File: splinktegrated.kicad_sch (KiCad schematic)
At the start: 55 parts, among them J1 USB_C_Receptacle_USB2.0, J10 NA_Ribbon, J11 NA_Serial, J12 NA_Conn_01x04_Female, J14 Cirque, J2 NA_Conn_01x04_Female, J3 NA_Conn_01x04_Female, J4 NA_Conn_01x04_Female, J5 Conn_01x02, J6 Cirque, J7 NA_trackball, J8 NA_Ribbon, J9 NA_RGB, SW1 NA_SW_SPST, SW2 NA_SW_SPST, U1 RP2040, U2 USBLC6-2P6, U3 XC6210B332MR-G, U4 USBLC6-2P6, U5 W25Q128JVS, Y1 Crystal_GND24

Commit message: add second jumper for full duplex
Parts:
- added NA_JP3, NA_JP4: NA_Jumper_2_Open, local-libraries:SolderJumper-2_P1.3mm_Open_RoundedPad1.0x1.5mm, symbol Jumper:Jumper_2_Open
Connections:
- net D12: now reaches U1.15 (GPIO12)
- net D12: now also NA_JP3.2 (B), NA_JP4.2 (B)
- net at NA_J6.T, NA_JP1.1 (A): now also J11.S, NA_JP4.1 (A)
- net at J11.T, NA_JP2.1 (A): now also NA_J6.S, NA_JP3.1 (A)
- no-connect marks 23 -> 20
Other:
- moved on the sheet: NA_JP1

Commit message: start implementing vik
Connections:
- net +3V3: no longer J6.1 (Pin_1)
- net GND: now also J6.11 (Pin_11); no longer J6.6 (Pin_6), J6.7 (Pin_7)
- net miso_l: now also J6.2 (Pin_2); no longer J6.5 (Pin_5), J6.8 (Pin_8)
- net mosi_l: now also J6.5 (Pin_5); no longer J6.10 (Pin_10), J6.3 (Pin_3)
- net rgb_r: now also J6.8 (Pin_8)
- net sc_l: now also J6.1 (Pin_1); no longer J6.4 (Pin_4), J6.9 (Pin_9)
- net ss_l: no longer J6.11 (Pin_11), J6.2 (Pin_2)
- net SDA: now reaches U1.4 (GPIO2)
- net SDA: now also J6.9 (Pin_9)
- net SCL: now reaches U1.5 (GPIO3)
- net SCL: now also J6.10 (Pin_10)
- no-connect marks 20 -> 19
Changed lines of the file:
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@@
 	)
 	(no_connect
-		(at 182.88 63.5)
-	)
-	(no_connect
-		(at 182.88 66.04)
-	)
-	(no_connect
 		(at 431.8 64.77)
 	)
@@
 		(at 391.16 67.31)
 	)
+	(no_connect
+		(at 431.8 46.99)
+	)
 	(polyline
 		(pts
@@
 	(global_label "ss_l"
 		(shape input)
-		(at 431.8 59.69 180)
+		(at 469.9 59.69 180)
 		(effects
 			(font
@@
 		)
 		(property "Intersheetrefs" "${INTERSHEET_REFS}"
-			(at 427.3307 59.6106 0)
+			(at 465.4307 59.6106 0)
 			(effects
 				(font
@@
 	(global_label "miso_l"
 		(shape input)
-		(at 431.8 44.45 180)
+		(at 431.8 59.69 180)
 		(effects
 			(font
@@
 		)
 		(property "Intersheetrefs" "${INTERSHEET_REFS}"
-			(at 424.9117 44.3706 0)
+			(at 424.9117 59.6106 0)
 			(effects
 				(font
@@
 	(global_label "mosi_l"
 		(shape input)
-		(at 431.8 57.15 180)
+		(at 469.9 57.15 180)
 		(effects
 			(font
@@
 		)
 		(property "Intersheetrefs" "${INTERSHEET_REFS}"
-			(at 424.9117 57.0706 0)
+			(at 463.0117 57.0706 0)
 			(effects
 				(font
@@
 		)
 	)
+	(global_label "SDA"
+		(shape input)
+		(at 182.88 63.5 0)
+		(effects
+			(font
+				(size 1.27 1.27)
+			)
+			(justify left)
+		)
+		(property "Intersheetrefs" "${INTERSHEET_REFS}"
+			(at 212.09 118.11 0)
+			(effects
+				(font
+					(size 1.27 1.27)
+				)
+				(hide yes)
+			)
+		)
+	)
 	(global_label "col3_l"
 		(shape input)
@@
 		)
 	)
+	(global_label "rgb_r"
+		(shape input)
+		(at 431.8 44.45 180)
+		(effects
+			(font
+				(size 1.27 1.27)
+			)
+			(justify right)
+		)
+		(property "Intersheetrefs" "${INTERSHEET_REFS}"
+			(at 344.17 -22.86 0)
+			(effects
+				(font
+					(size 1.27 1.27)
+				)
+				(hide yes)
+			)
+		)
+	)
 	(global_label "ss_l"
 		(shape input)
@@
 	(global_label "sc_l"
 		(shape input)
-		(at 431.8 41.91 180)
+		(at 431.8 62.23 180)
 		(effects
 			(font
@@
 		)
 		(property "Intersheetrefs" "${INTERSHEET_REFS}"
-			(at 427.2702 41.8306 0)
+			(at 427.2702 62.1506 0)
 			(effects
 				(font
@@
 		)
 	)
+	(global_label "SDA"
+		(shape input)
+		(at 431.8 41.91 180)
+		(effects
+			(font
+				(size 1.27 1.27)
+			)
+			(justify right)
+		)
+		(property "Intersheetrefs" "${INTERSHEET_REFS}"
+			(at 402.59 -12.7 0)
+			(effects
+				(font
+					(size 1.27 1.27)
+				)
+				(hide yes)
+			)
+		)
+	)
 	(global_label "sc_l"
 		(shape input)
-		(at 431.8 54.61 180)
+		(at 469.9 54.61 180)
 		(effects
 			(font
@@
 		)
 		(property "Intersheetrefs" "${INTERSHEET_REFS}"
-			(at 427.2702 54.5306 0)
+			(at 465.3702 54.5306 0)
 			(effects
 				(font
@@
 		)
 	)
+	(global_label "SCL"
+		(shape input)
+		(at 182.88 66.04 0)
+		(effects
+			(font
+				(size 1.27 1.27)
+			)
+			(justify left)
+		)
+		(property "Intersheetrefs" "${INTERSHEET_REFS}"
+			(at 212.09 120.65 0)
+			(effects
+				(font
+					(size 1.27 1.27)
+				)
+				(hide yes)
+			)
+		)
+	)
 	(global_label "mosi_l"
 		(shape input)
-		(at 431.8 39.37 180)
+		(at 431.8 52.07 180)
 		(effects
 			(font
@@
 		)
 		(property "Intersheetrefs" "${INTERSHEET_REFS}"
-			(at 424.9117 39.2906 0)
+			(at 424.9117 51.9906 0)
 			(effects
 				(font
@@
 	(global_label "miso_l"
 		(shape input)
-		(at 431.8 52.07 180)
+		(at 469.9 52.07 180)
 		(effects
 			(font
@@
 		)
 		(property "Intersheetrefs" "${INTERSHEET_REFS}"
-			(at 424.9117 51.9906 0)
+			(at 463.0117 51.9906 0)
 			(effects
 				(font
@@
 		)
 	)
+	(global_label "SCL"
+		(shape input)
+		(at 431.8 39.37 180)
+		(effects
+			(font
+				(size 1.27 1.27)
+			)
+			(justify right)
+		)
+		(property "Intersheetrefs" "${INTERSHEET_REFS}"
+			(at 402.59 -15.24 0)
+			(effects
+				(font
+					(size 1.27 1.27)
+				)
+				(hide yes)
+			)
+		)
+	)
 	(global_label "row3_l"
 		(shape input)
@@
 	(global_label "ss_l"
 		(shape input)
-		(at 431.8 36.83 180)
+		(at 469.9 36.83 180)
 		(effects
 			(font
@@
 		)
 		(property "Intersheetrefs" "${INTERSHEET_REFS}"
-			(at 427.3307 36.7506 0)
+			(at 465.4307 36.7506 0)
 			(effects
 				(font
@@
 	(symbol
 		(lib_id "power:GND")
-		(at 431.8 49.53 270)
+		(at 469.9 49.53 270)
 		(unit 1)
 		(exclude_from_sim no)
@@
 		(dnp no)
 		(property "Reference" "#PWR039"
-			(at 425.45 49.53 0)
+			(at 463.55 49.53 0)
 			(effects
 				(font
@@
 		)
 		(property "Value" "GND"
-			(at 425.45 49.53 90)
+			(at 463.55 49.53 90)
 			(effects
 				(font
@@
 		)
 		(property "Footprint" ""
-			(at 431.8 49.53 0)
+			(at 469.9 49.53 0)
 			(effects
 				(font
@@
 		)
 		(property "Datasheet" ""
-			(at 431.8 49.53 0)
+			(at 469.9 49.53 0)
 			(effects
 				(font
@@
 		)
 		(property "Description" ""
-			(at 431.8 49.53 0)
+			(at 469.9 49.53 0)
 			(effects
 				(font
@@
 	(symbol
 		(lib_id "power:GND")
-		(at 431.8 46.99 270)
+		(at 431.8 36.83 270)
 		(unit 1)
 		(exclude_from_sim no)
@@
 		(dnp no)
 		(property "Reference" "#PWR037"
-			(at 425.45 46.99 0)
+			(at 425.45 36.83 0)
 			(effects
 				(font
@@
 		)
 		(property "Value" "GND"
-			(at 425.45 46.99 90)
+			(at 425.45 36.83 90)
 			(effects
 				(font
@@
 		)
 		(property "Footprint" ""
-			(at 431.8 46.99 0)
+			(at 431.8 36.83 0)
 			(effects
 				(font
@@
 		)
 		(property "Datasheet" ""
-			(at 431.8 46.99 0)
+			(at 431.8 36.83 0)
 			(effects
 				(font
@@
 		)
 		(property "Description" ""
-			(at 431.8 46.99 0)
+			(at 431.8 36.83 0)
 			(effects
 				(font
@@
 	(symbol
 		(lib_id "power:+3.3V")
-		(at 431.8 62.23 90)
+		(at 458.47 69.85 90)
 		(unit 1)
 		(exclude_from_sim no)
@@
 		(dnp no)
 		(property "Reference" "#PWR040"
-			(at 435.61 62.23 0)
+			(at 462.28 69.85 0)
 			(effects
 				(font
@@
 		)
 		(property "Value" "+3V3"
-			(at 427.99 62.23 0)
+			(at 461.01 69.85 0)
 			(effects
 				(font
@@
 		)
 		(property "Footprint" ""
-			(at 431.8 62.23 0)
+			(at 458.47 69.85 0)
 			(effects
 				(font
@@
 		)
 		(property "Datasheet" ""
-			(at 431.8 62.23 0)
+			(at 458.47 69.85 0)
 			(effects
 				(font
@@
 		)
 		(property "Description" ""
-			(at 431.8 62.23 0)
+			(at 458.47 69.85 0)
 			(effects
 				(font

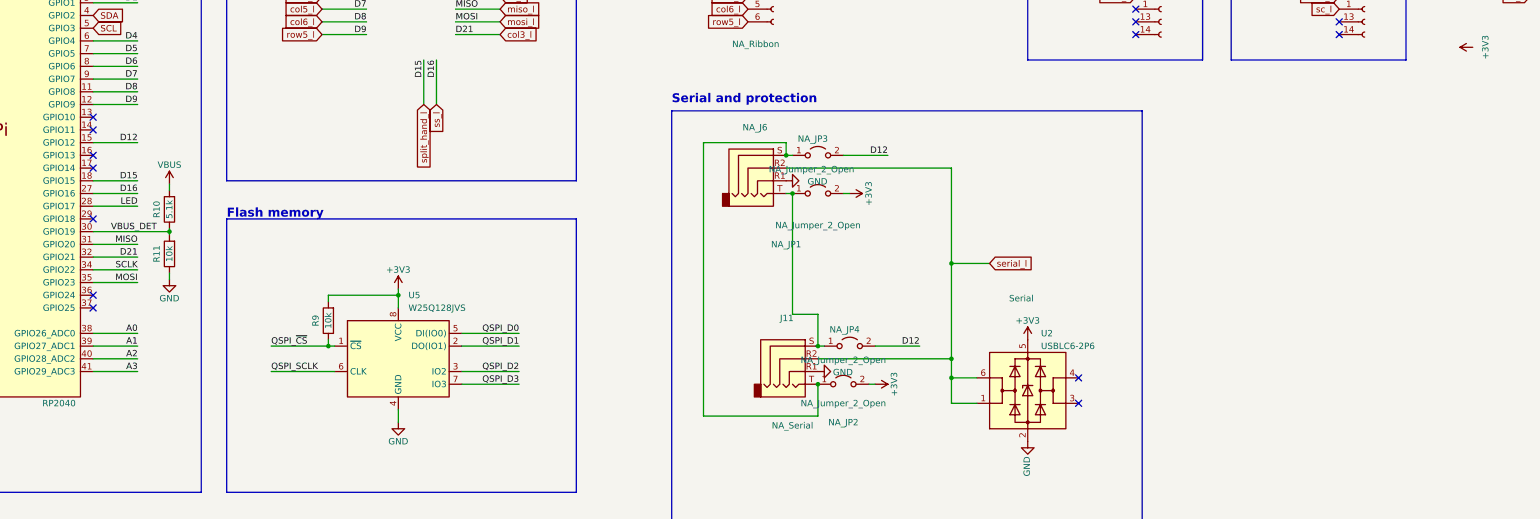
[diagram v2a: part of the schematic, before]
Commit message: add criss crossed jumpers for full duplex
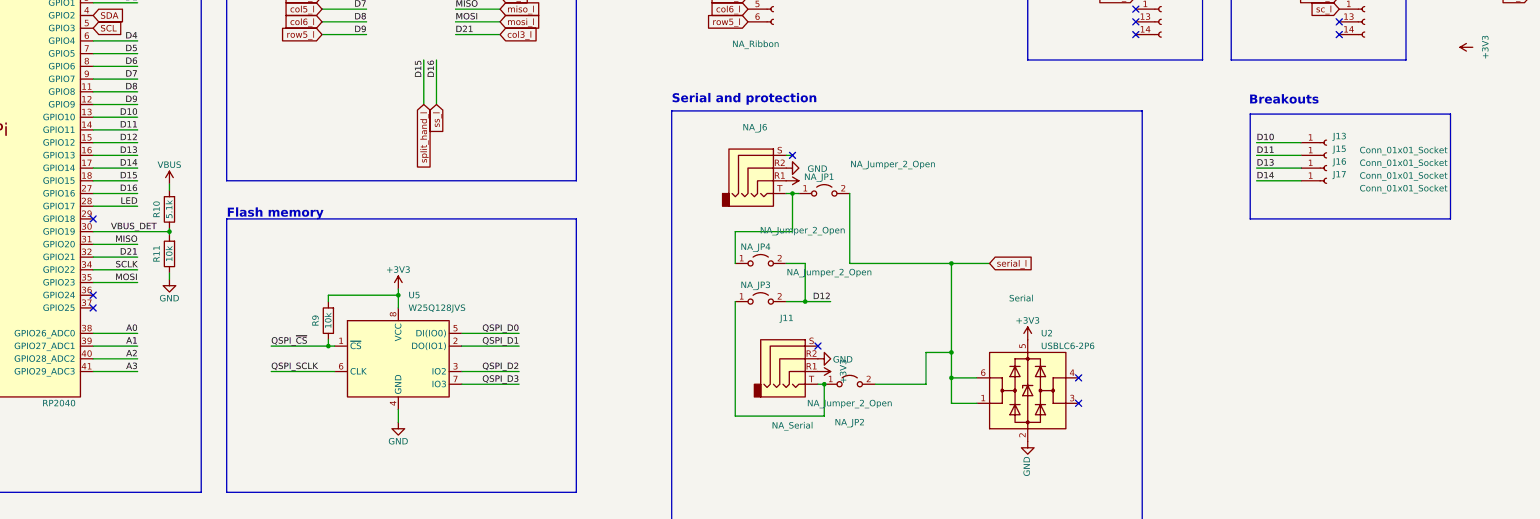
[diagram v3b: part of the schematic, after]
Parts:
- added J13, J15, J16, J17: Conn_01x01_Socket, local-libraries:PinHeader_1x01_P1.27mm_Vertical, symbol Connector:Conn_01x01_Socket
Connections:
- net +3V3: now also J11.R1, NA_J6.R1; no longer NA_JP1.2 (B), NA_JP2.2 (B)
- net GND: now also J11.R2, NA_J6.R2; no longer J11.R1, NA_J6.R1
- net serial_l: now also NA_JP1.2 (B), NA_JP2.2 (B); no longer J11.R2, NA_J6.R2
- net D10: now reaches U1.13 (GPIO10)
- net D10: now also J13.1 (Pin_1)
- net D11: now reaches U1.14 (GPIO11)
- net D11: now also J15.1 (Pin_1)
- net D13: now reaches U1.16 (GPIO13)
- net D13: now also J16.1 (Pin_1)
- net D14: now reaches U1.17 (GPIO14)
- net D14: now also J17.1 (Pin_1)
- net at NA_J6.T, NA_JP1.1 (A), NA_JP4.1 (A): no longer J11.S
- net at J11.T, NA_JP2.1 (A), NA_JP3.1 (A): no longer NA_J6.S
- no-connect marks 19 -> 17
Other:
- note added: "Breakouts"
- moved on the sheet: NA_JP2, NA_JP3, NA_JP4

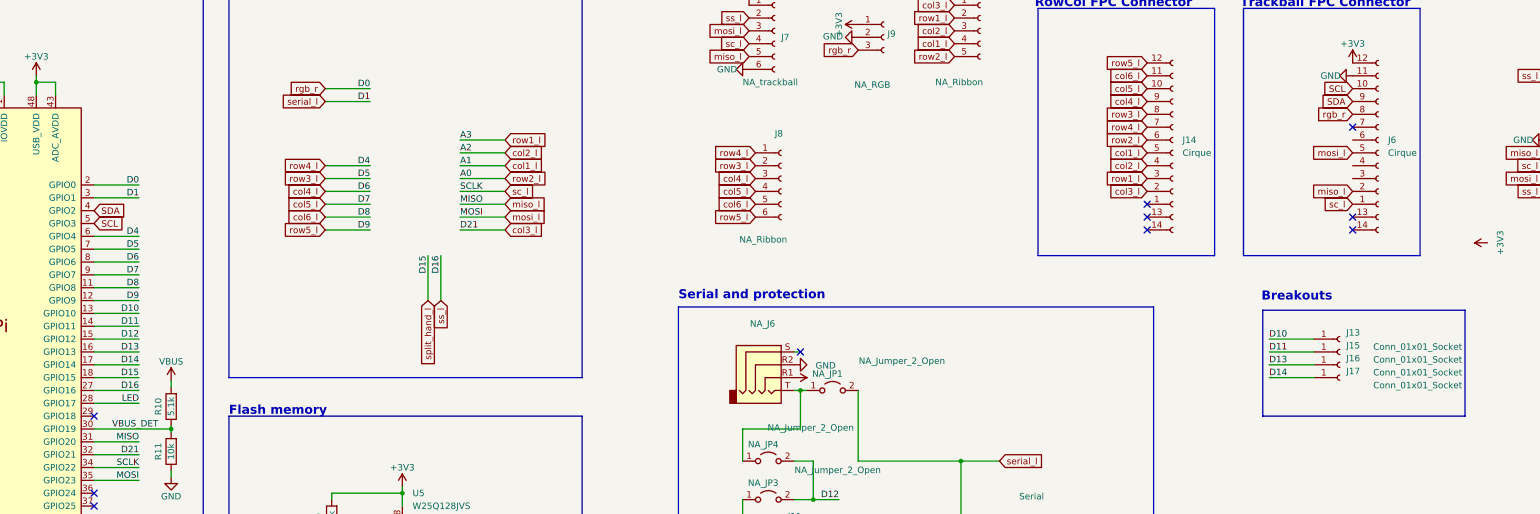
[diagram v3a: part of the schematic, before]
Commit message: add 5v jumper
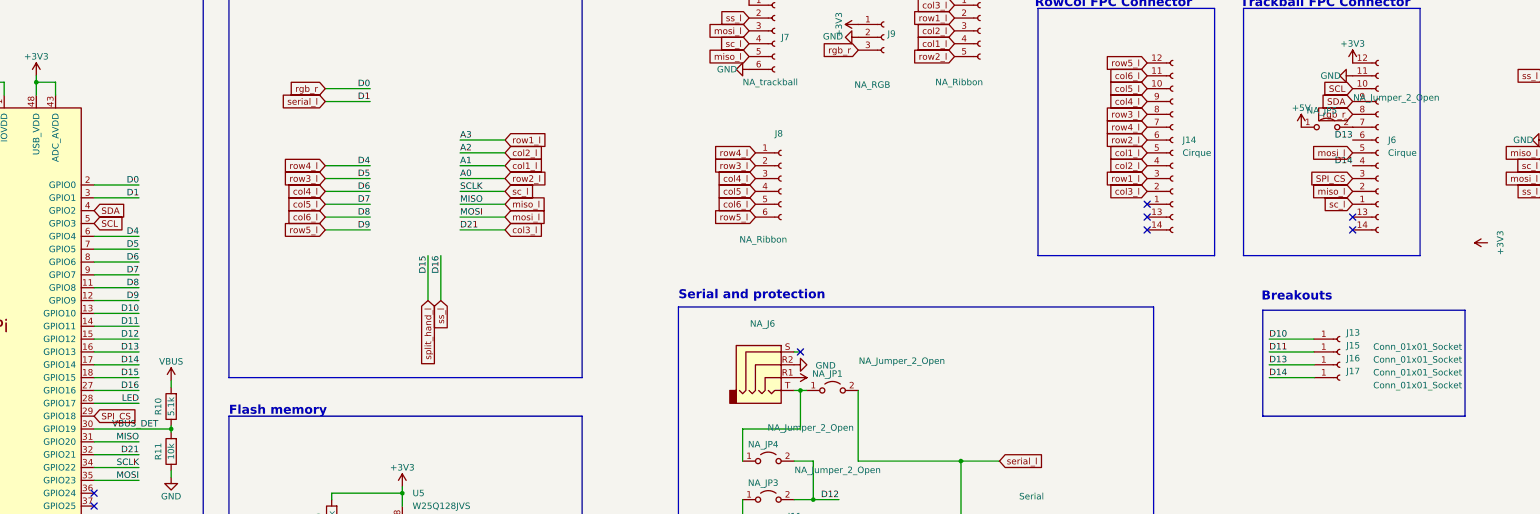
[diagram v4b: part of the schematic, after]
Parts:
- added NA_JP5: NA_Jumper_2_Open, local-libraries:SolderJumper-2_P1.3mm_Open_RoundedPad1.0x1.5mm, symbol Jumper:Jumper_2_Open
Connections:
- net +5V: now also NA_JP5.1 (A)
- net D13: now also J6.6 (Pin_6)
- net D14: now also J6.4 (Pin_4)
- net SPI_CS: now reaches U1.29 (GPIO18)
- net SPI_CS: now also J6.3 (Pin_3)
- net at J6.7 (Pin_7): now also NA_JP5.2 (B)
- no-connect marks 17 -> 15
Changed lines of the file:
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@@
 	)
 	(no_connect
-		(at 182.88 104.14)
-	)
-	(no_connect
 		(at 391.16 62.23)
 	)
@@
 		(at 391.16 67.31)
 	)
-	(no_connect
-		(at 431.8 46.99)
-	)
 	(polyline
 		(pts
@@
 		)
 	)
+	(label "D13"
+		(at 431.8 49.53 180)
+		(fields_autoplaced yes)
+		(effects
+			(font
+				(size 1.27 1.27)
+			)
+			(justify right bottom)
+		)
+	)
 	(label "QSPI_D2"
 		(at 111.76 68.58 0)
@@
 		)
 	)
+	(label "D14"
+		(at 431.8 54.61 180)
+		(fields_autoplaced yes)
+		(effects
+			(font
+				(size 1.27 1.27)
+			)
+			(justify right bottom)
+		)
+	)
 	(label "D+_daughter"
 		(at -66.675 87.63 180)
@@
 		)
 	)
+	(global_label "SPI_CS"
+		(shape input)
+		(at 431.8 57.15 180)
+		(effects
+			(font
+				(size 1.27 1.27)
+			)
+			(justify right)
+		)
+		(property "Intersheetrefs" "${INTERSHEET_REFS}"
+			(at 402.59 17.78 0)
+			(effects
+				(font
+					(size 1.27 1.27)
+				)
+				(hide yes)
+			)
+		)
+	)
 	(global_label "col4_l"
 		(shape input)
@@
 		)
 	)
+	(global_label "SPI_CS"
+		(shape input)
+		(at 182.88 104.14 0)
+		(effects
+			(font
+				(size 1.27 1.27)
+			)
+			(justify left)
+		)
+		(property "Intersheetrefs" "${INTERSHEET_REFS}"
+			(at 212.09 143.51 0)
+			(effects
+				(font
+					(size 1.27 1.27)
+				)
+				(hide yes)
+			)
+		)
+	)
 	(global_label "row2_l"
 		(shape input)
@@
 	)
 	(symbol
+		(lib_id "power:+5V")
+		(at 421.64 46.99 0)
+		(unit 1)
+		(exclude_from_sim no)
+		(in_bom yes)
+		(on_board yes)
+		(dnp no)
+		(property "Reference" "#PWR041"
+			(at 421.64 50.8 0)
+			(effects
+				(font
+					(size 1.27 1.27)
+				)
+				(hide yes)
+			)
+		)
+		(property "Value" "+5V"
+			(at 421.64 43.18 0)
+			(effects
+				(font
+					(size 1.27 1.27)
+				)
+			)
+		)
+		(property "Footprint" ""
+			(at 421.64 46.99 0)
+			(effects
+				(font
+					(size 1.27 1.27)
+				)
+				(hide yes)
+			)
+		)
+		(property "Datasheet" ""
+			(at 421.64 46.99 0)
+			(effects
+				(font
+					(size 1.27 1.27)
+				)
+				(hide yes)
+			)
+		)
+		(property "Description" ""
+			(at 421.64 46.99 0)
+			(effects
+				(font
+					(size 1.27 1.27)
+				)
+				(hide yes)
+			)
+		)
+		(pin "1"
+		)
+		(instances
+			(project "splinktegrated"
+				(path "/7353e96a-343a-4876-b497-b1d205a14d97"
+					(reference "#PWR041")
+					(unit 1)
+				)
+			)
+		)
+	)
+	(symbol
 		(lib_id "Connector:Conn_01x04_Female")
 		(at 41.91 40.005 0)
@@
 					(unit 1)
 				)
+			)
+		)
+	)
+	(symbol
+		(lib_id "Jumper:Jumper_2_Open")
+		(at 426.72 46.99 0)
+		(unit 1)
+		(exclude_from_sim no)
+		(in_bom no)
+		(on_board yes)
+		(dnp no)
+		(property "Reference" "NA_JP5"
+			(at 425.704 43.688 0)
+			(effects
+				(font
+					(size 1.27 1.27)
+				)
+			)
+		)
+		(property "Value" "NA_Jumper_2_Open"
+			(at 440.436 41.148 0)
+			(effects
+				(font
+					(size 1.27 1.27)
+				)
+			)
+		)
+		(property "Footprint" "local-libraries:SolderJumper-2_P1.3mm_Open_RoundedPad1.0x1.5mm"
+			(at 426.72 46.99 0)
+			(effects
+				(font
+					(size 1.27 1.27)
+				)
+				(hide yes)
+			)
+		)
+		(property "Datasheet" "~"
+			(at 426.72 46.99 0)
+			(effects
+				(font
+					(size 1.27 1.27)
+				)
+				(hide yes)
+			)
+		)
+		(property "Description" ""
+			(at 426.72 46.99 0)
+			(effects
+				(font
+					(size 1.27 1.27)
+				)
+				(hide yes)
+			)
+		)
+		(pin "1"
+		)
+		(pin "2"
+		)
+		(instances
+			(project "splinktegrated"
+				(path "/7353e96a-343a-4876-b497-b1d205a14d97"
+					(reference "NA_JP5")
+					(unit 1)
+				)

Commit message: routing
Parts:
- removed J13, J15: Conn_01x01_Socket, local-libraries:PinHeader_1x01_P1.27mm_Vertical, symbol Connector:Conn_01x01_Socket
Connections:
- net D10: no longer names the net of U1.13 (GPIO10)
- net D11: no longer names the net of U1.14 (GPIO11)
- net split_hand_l: no longer names the net of U1.18 (GPIO15)
- no-connect marks 15 -> 18
